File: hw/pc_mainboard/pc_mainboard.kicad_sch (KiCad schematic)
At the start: 0 parts

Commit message: Research for serial interface
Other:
- sheet ethernet renamed phy
- removed sheet program
- added sheet serial (serial.kicad_sch)
- sheet phy: file ethernet.kicad_sch -> phy.kicad_sch
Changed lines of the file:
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@@
 	(generator "eeschema")
 	(generator_version "8.0")
-	(paper "A4")
+	(paper "A2")
 	(title_block
 		(title "Mainboard")
 	)
 	(sheet
-		(at 53.34 81.28)
-		(size 36.83 29.21)
-		(fields_autoplaced yes)
-		(stroke
-			(width 0.1524)
-			(type solid)
-		)
-		(fill
-			(color 0 0 0 0.0000)
-		)
-		(property "Sheetname" "program"
-			(at 53.34 80.5684 0)
-			(effects
-				(font
-					(size 1.27 1.27)
-				)
-				(justify left bottom)
-			)
-		)
-		(property "Sheetfile" "program.kicad_sch"
-			(at 53.34 111.0746 0)
-			(effects
-				(font
-					(size 1.27 1.27)
-				)
-				(justify left top)
-			)
-		)
-		(instances
-			(project "pc_mainboard"
-				(path "/69a74940-cd00-4a75-bd5b-2bda9e86219a"
-					(page "8")
-				)
-			)
-		)
-	)
-	(sheet
-		(at 172.72 130.81)
+		(at 335.28 231.14)
 		(size 25.4 21.59)
 		(fields_autoplaced yes)
@@
 			(color 0 0 0 0.0000)
 		)
-		(property "Sheetname" "ethernet"
-			(at 172.72 130.0984 0)
-			(effects
-				(font
-					(size 1.27 1.27)
-				)
-				(justify left bottom)
-			)
-		)
-		(property "Sheetfile" "ethernet.kicad_sch"
-			(at 172.72 152.9846 0)
+		(property "Sheetname" "phy"
+			(at 335.28 230.4284 0)
+			(effects
+				(font
+					(size 1.27 1.27)
+				)
+				(justify left bottom)
+			)
+		)
+		(property "Sheetfile" "phy.kicad_sch"
+			(at 335.28 253.3146 0)
 			(effects
 				(font
@@
 	)
 	(sheet
-		(at 45.72 29.21)
+		(at 208.28 129.54)
 		(size 31.75 31.75)
 		(fields_autoplaced yes)
@@
 		)
 		(property "Sheetname" "power"
-			(at 45.72 28.4984 0)
+			(at 208.28 128.8284 0)
 			(effects
 				(font
@@
 		)
 		(property "Sheetfile" "power.kicad_sch"
-			(at 45.72 61.5446 0)
+			(at 208.28 161.8746 0)
 			(effects
 				(font
@@
 	)
 	(sheet
-		(at 134.62 29.21)
+		(at 297.18 129.54)
 		(size 36.83 31.75)
 		(fields_autoplaced yes)
@@
 		)
 		(property "Sheetname" "peripherals"
-			(at 134.62 28.4984 0)
+			(at 297.18 128.8284 0)
 			(effects
 				(font
@@
 		)
 		(property "Sheetfile" "peripherals.kicad_sch"
-			(at 134.62 61.5446 0)
+			(at 297.18 161.8746 0)
 			(effects
 				(font
@@
 	)
 	(sheet
-		(at 172.72 76.2)
+		(at 335.28 176.53)
 		(size 50.8 40.64)
 		(fields_autoplaced yes)
@@
 		)
 		(property "Sheetname" "flash"
-			(at 172.72 75.4884 0)
+			(at 335.28 175.8184 0)
 			(effects
 				(font
@@
 		)
 		(property "Sheetfile" "flash.kicad_sch"
-			(at 172.72 117.4246 0)
+			(at 335.28 217.7546 0)
 			(effects
 				(font
@@
 	)
 	(sheet
-		(at 111.76 76.2)
+		(at 274.32 176.53)
 		(size 45.72 40.64)
 		(fields_autoplaced yes)
@@
 		)
 		(property "Sheetname" "mpu"
-			(at 111.76 75.4884 0)
+			(at 274.32 175.8184 0)
 			(effects
 				(font
@@
 		)
 		(property "Sheetfile" "mpu.kicad_sch"
-			(at 111.76 117.4246 0)
+			(at 274.32 217.7546 0)
 			(effects
 				(font
@@
 	)
 	(sheet
-		(at 87.63 29.21)
+		(at 222.25 184.15)
+		(size 31.75 29.21)
+		(fields_autoplaced yes)
+		(stroke
+			(width 0.1524)
+			(type solid)
+		)
+		(fill
+			(color 0 0 0 0.0000)
+		)
+		(property "Sheetname" "serial"
+			(at 222.25 183.4384 0)
+			(effects
+				(font
+					(size 1.27 1.27)
+				)
+				(justify left bottom)
+			)
+		)
+		(property "Sheetfile" "serial.kicad_sch"
+			(at 222.25 213.9446 0)
+			(effects
+				(font
+					(size 1.27 1.27)
+				)
+				(justify left top)
+			)
+		)
+		(instances
+			(project "pc_mainboard"
+				(path "/69a74940-cd00-4a75-bd5b-2bda9e86219a"
+					(page "9")
+				)
+			)
+		)
+	)
+	(sheet
+		(at 250.19 129.54)
 		(size 38.1 31.75)
 		(fields_autoplaced yes)
@@
 		)
 		(property "Sheetname" "external"
-			(at 87.63 28.4984 0)
+			(at 250.19 128.8284 0)
 			(effects
 				(font
@@
 		)
 		(property "Sheetfile" "external.kicad_sch"
-			(at 87.63 61.5446 0)
+			(at 250.19 161.8746 0)
 			(effects
 				(font
@@
 	)
 	(sheet
-		(at 115.57 130.81)
+		(at 278.13 231.14)
 		(size 35.56 21.59)
 		(fields_autoplaced yes)
@@
 		)
 		(property "Sheetname" "ram"
-			(at 115.57 130.0984 0)
+			(at 278.13 230.4284 0)
 			(effects
 				(font
@@
 		)
 		(property "Sheetfile" "ram.kicad_sch"
-			(at 115.57 152.9846 0)
-			(effects
-				(font
+			(at 278.13 253.3146 0)
+			(effects
+				(font

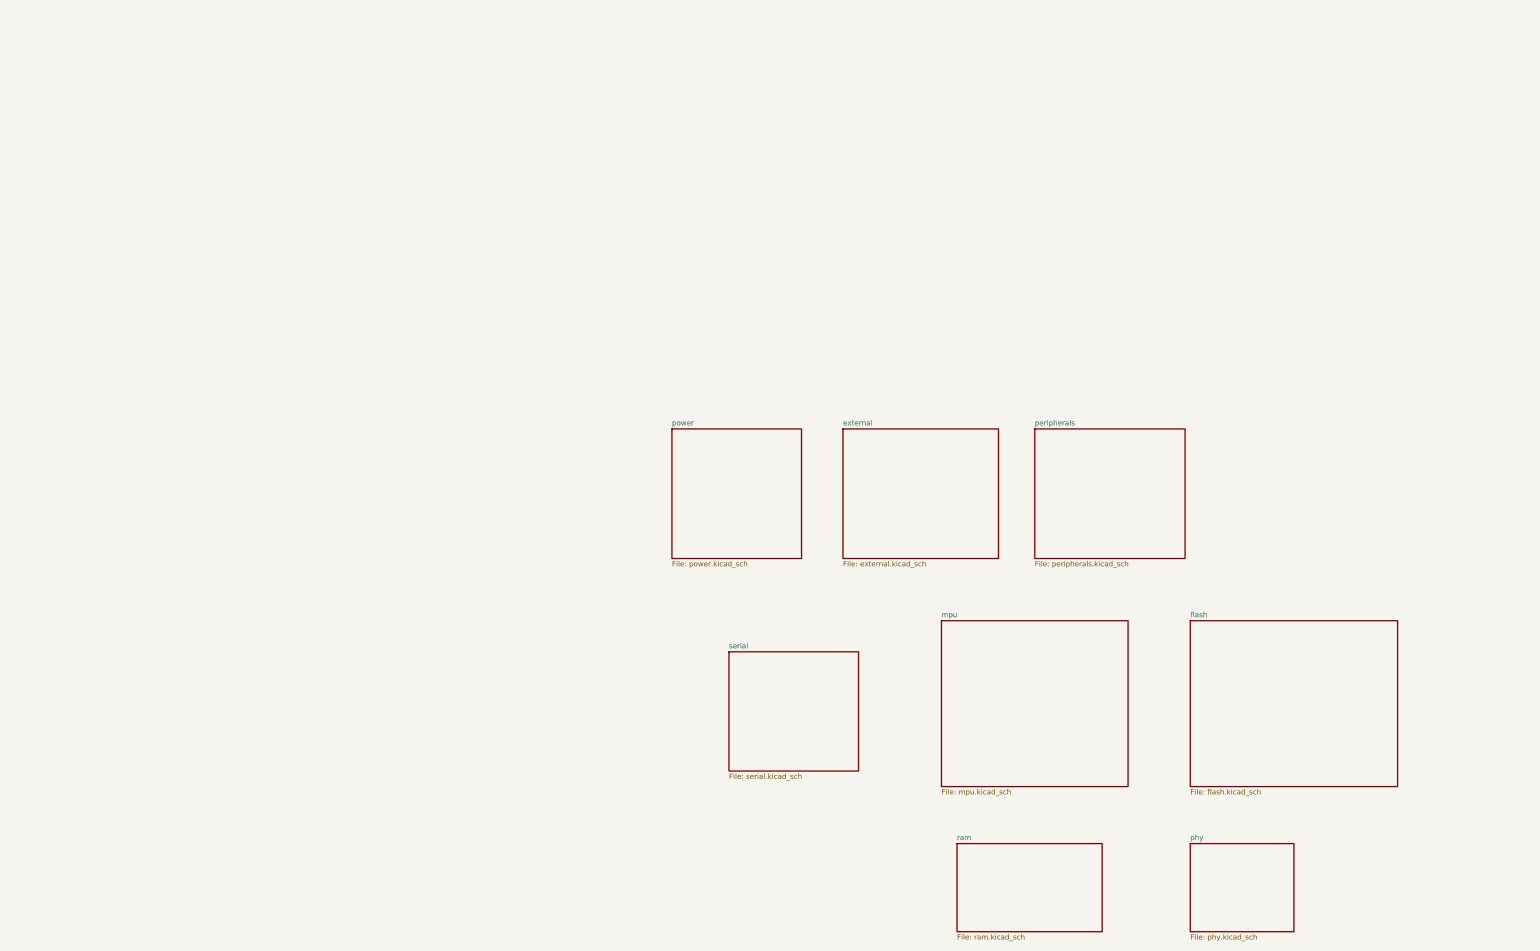
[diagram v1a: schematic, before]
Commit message: Added RTC (#22)
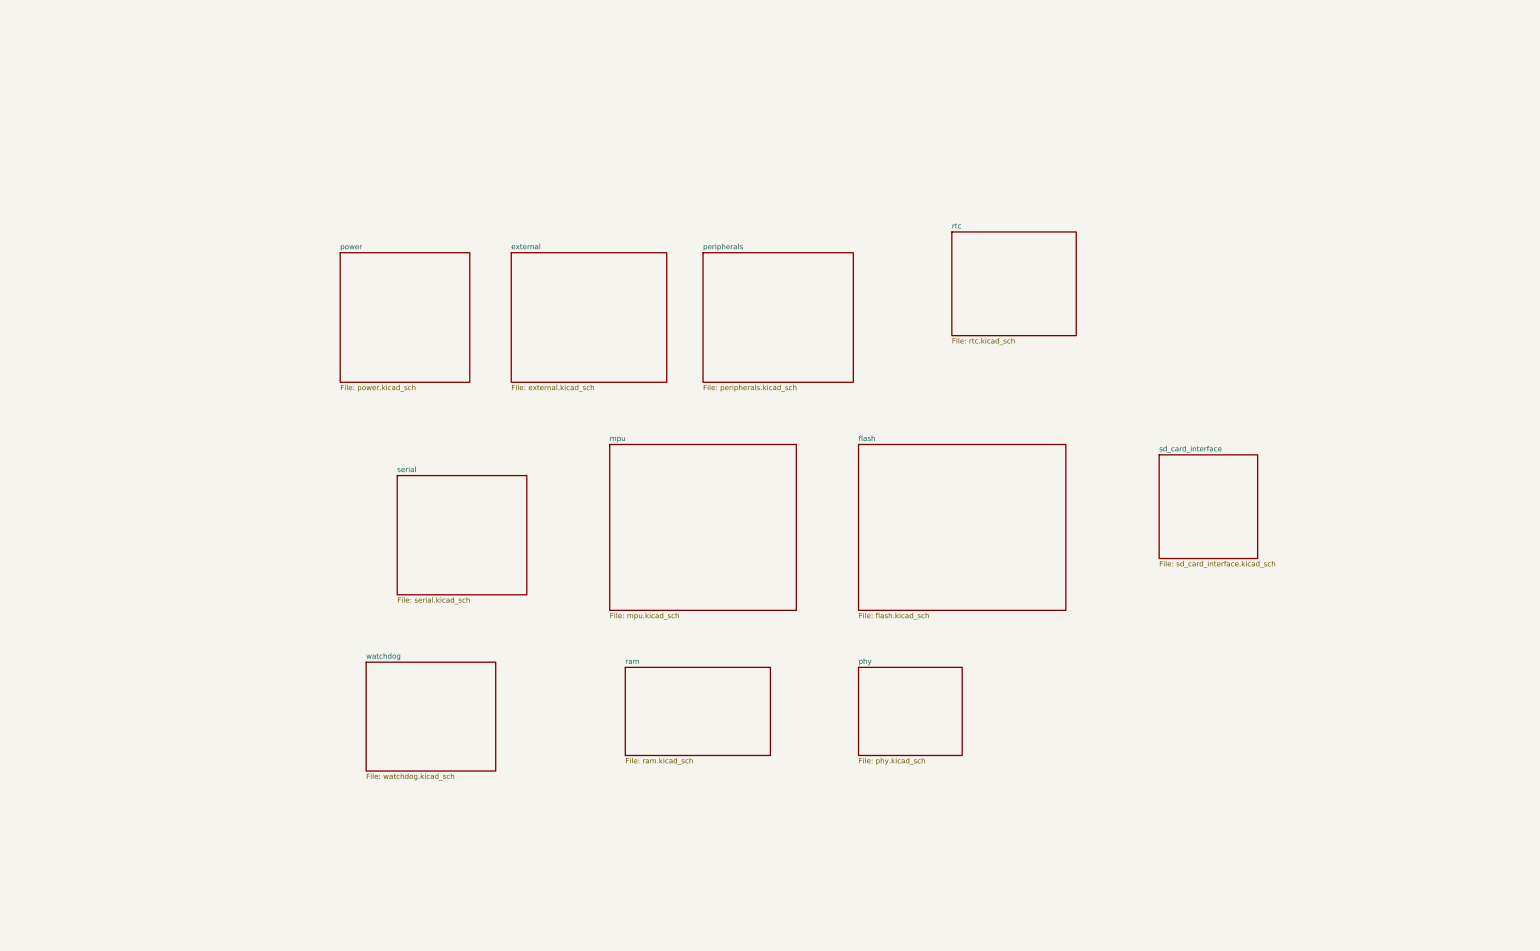
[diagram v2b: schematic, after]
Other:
- added sheet rtc (rtc.kicad_sch)
- added sheet sd_card_interface (sd_card_interface.kicad_sch)
- added sheet watchdog (watchdog.kicad_sch)
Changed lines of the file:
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@@
 	(generator "eeschema")
 	(generator_version "8.0")
-	(paper "A2")
+	(paper "B")
 	(title_block
 		(title "Mainboard")
 	)
 	(sheet
-		(at 335.28 231.14)
+		(at 276.86 81.28)
+		(size 30.48 25.4)
+		(fields_autoplaced yes)
+		(stroke
+			(width 0.1524)
+			(type solid)
+		)
+		(fill
+			(color 0 0 0 0.0000)
+		)
+		(property "Sheetname" "rtc"
+			(at 276.86 80.5684 0)
+			(effects
+				(font
+					(size 1.27 1.27)
+				)
+				(justify left bottom)
+			)
+		)
+		(property "Sheetfile" "rtc.kicad_sch"
+			(at 276.86 107.2646 0)
+			(effects
+				(font
+					(size 1.27 1.27)
+				)
+				(justify left top)
+			)
+		)
+		(instances
+			(project "pc_mainboard"
+				(path "/69a74940-cd00-4a75-bd5b-2bda9e86219a"
+					(page "10")
+				)
+			)
+		)
+	)
+	(sheet
+		(at 254 187.96)
 		(size 25.4 21.59)
 		(fields_autoplaced yes)
@@
 		)
 		(property "Sheetname" "phy"
-			(at 335.28 230.4284 0)
+			(at 254 187.2484 0)
 			(effects
 				(font
@@
 		)
 		(property "Sheetfile" "phy.kicad_sch"
-			(at 335.28 253.3146 0)
+			(at 254 210.1346 0)
 			(effects
 				(font
@@
 	)
 	(sheet
-		(at 208.28 129.54)
+		(at 327.66 135.89)
+		(size 24.13 25.4)
+		(fields_autoplaced yes)
+		(stroke
+			(width 0.1524)
+			(type solid)
+		)
+		(fill
+			(color 0 0 0 0.0000)
+		)
+		(property "Sheetname" "sd_card_interface"
+			(at 327.66 135.1784 0)
+			(effects
+				(font
+					(size 1.27 1.27)
+				)
+				(justify left bottom)
+			)
+		)
+		(property "Sheetfile" "sd_card_interface.kicad_sch"
+			(at 327.66 161.8746 0)
+			(effects
+				(font
+					(size 1.27 1.27)
+				)
+				(justify left top)
+			)
+		)
+		(instances
+			(project "pc_mainboard"
+				(path "/69a74940-cd00-4a75-bd5b-2bda9e86219a"
+					(page "12")
+				)
+			)
+		)
+	)
+	(sheet
+		(at 127 86.36)
 		(size 31.75 31.75)
 		(fields_autoplaced yes)
@@
 		)
 		(property "Sheetname" "power"
-			(at 208.28 128.8284 0)
+			(at 127 85.6484 0)
 			(effects
 				(font
@@
 		)
 		(property "Sheetfile" "power.kicad_sch"
-			(at 208.28 161.8746 0)
+			(at 127 118.6946 0)
 			(effects
 				(font
@@
 	)
 	(sheet
-		(at 297.18 129.54)
+		(at 215.9 86.36)
 		(size 36.83 31.75)
 		(fields_autoplaced yes)
@@
 		)
 		(property "Sheetname" "peripherals"
-			(at 297.18 128.8284 0)
+			(at 215.9 85.6484 0)
 			(effects
 				(font
@@
 		)
 		(property "Sheetfile" "peripherals.kicad_sch"
-			(at 297.18 161.8746 0)
+			(at 215.9 118.6946 0)
 			(effects
 				(font
@@
 	)
 	(sheet
-		(at 335.28 176.53)
+		(at 254 133.35)
 		(size 50.8 40.64)
 		(fields_autoplaced yes)
@@
 		)
 		(property "Sheetname" "flash"
-			(at 335.28 175.8184 0)
+			(at 254 132.6384 0)
 			(effects
 				(font
@@
 		)
 		(property "Sheetfile" "flash.kicad_sch"
-			(at 335.28 217.7546 0)
+			(at 254 174.5746 0)
 			(effects
 				(font
@@
 	)
 	(sheet
-		(at 274.32 176.53)
+		(at 133.35 186.69)
+		(size 31.75 26.67)
+		(fields_autoplaced yes)
+		(stroke
+			(width 0.1524)
+			(type solid)
+		)
+		(fill
+			(color 0 0 0 0.0000)
+		)
+		(property "Sheetname" "watchdog"
+			(at 133.35 185.9784 0)
+			(effects
+				(font
+					(size 1.27 1.27)
+				)
+				(justify left bottom)
+			)
+		)
+		(property "Sheetfile" "watchdog.kicad_sch"
+			(at 133.35 213.9446 0)
+			(effects
+				(font
+					(size 1.27 1.27)
+				)
+				(justify left top)
+			)
+		)
+		(instances
+			(project "pc_mainboard"
+				(path "/69a74940-cd00-4a75-bd5b-2bda9e86219a"
+					(page "11")
+				)
+			)
+		)
+	)
+	(sheet
+		(at 193.04 133.35)
 		(size 45.72 40.64)
 		(fields_autoplaced yes)
@@
 		)
 		(property "Sheetname" "mpu"
-			(at 274.32 175.8184 0)
+			(at 193.04 132.6384 0)
 			(effects
 				(font
@@
 		)
 		(property "Sheetfile" "mpu.kicad_sch"
-			(at 274.32 217.7546 0)
+			(at 193.04 174.5746 0)
 			(effects
 				(font
@@
 	)
 	(sheet
-		(at 222.25 184.15)
+		(at 140.97 140.97)
 		(size 31.75 29.21)
 		(fields_autoplaced yes)
@@
 		)
 		(property "Sheetname" "serial"
-			(at 222.25 183.4384 0)
+			(at 140.97 140.2584 0)
 			(effects
 				(font
@@
 		)
 		(property "Sheetfile" "serial.kicad_sch"
-			(at 222.25 213.9446 0)
+			(at 140.97 170.7646 0)
 			(effects
 				(font
@@
 	)
 	(sheet
-		(at 250.19 129.54)
+		(at 168.91 86.36)
 		(size 38.1 31.75)
 		(fields_autoplaced yes)
@@
 		)
 		(property "Sheetname" "external"
-			(at 250.19 128.8284 0)
+			(at 168.91 85.6484 0)
 			(effects
 				(font
@@
 		)
 		(property "Sheetfile" "external.kicad_sch"
-			(at 250.19 161.8746 0)
+			(at 168.91 118.6946 0)
 			(effects
 				(font
@@
 	)
 	(sheet
-		(at 278.13 231.14)
+		(at 196.85 187.96)
 		(size 35.56 21.59)
 		(fields_autoplaced yes)
@@
 		)
 		(property "Sheetname" "ram"
-			(at 278.13 230.4284 0)
+			(at 196.85 187.2484 0)
 			(effects
 				(font
@@
 		)
 		(property "Sheetfile" "ram.kicad_sch"
-			(at 278.13 253.3146 0)
-			(effects
-				(font
+			(at 196.85 210.1346 0)
+			(effects
+				(font

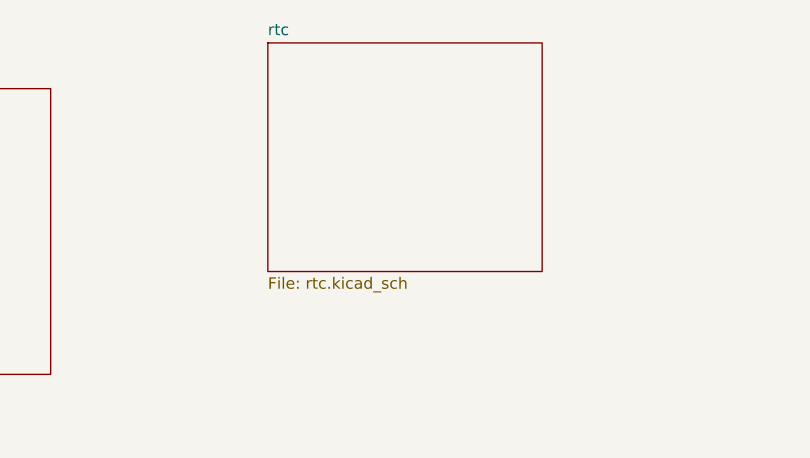
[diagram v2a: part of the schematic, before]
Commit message: RTC Schematic Capture (#35)
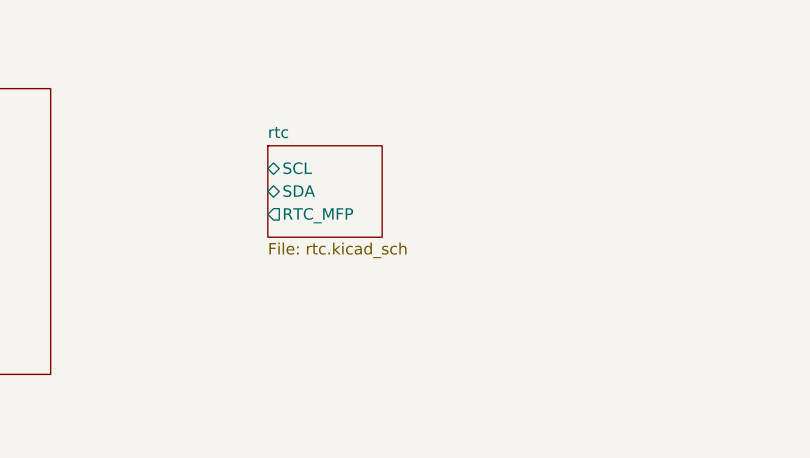
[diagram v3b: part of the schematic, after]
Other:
- sheet rtc ports: added RTC_MFP, SCL, SDA; removed none
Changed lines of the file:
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@@
 	)
 	(sheet
-		(at 276.86 81.28)
-		(size 30.48 25.4)
+		(at 276.86 92.71)
+		(size 12.7 10.16)
 		(fields_autoplaced yes)
 		(stroke
@@
 		)
 		(property "Sheetname" "rtc"
-			(at 276.86 80.5684 0)
+			(at 276.86 91.9984 0)
 			(effects
 				(font
@@
 		)
 		(property "Sheetfile" "rtc.kicad_sch"
-			(at 276.86 107.2646 0)
+			(at 276.86 103.4546 0)
 			(effects
 				(font
@@
 			)
 		)
+		(pin "RTC_MFP" output
+			(at 276.86 100.33 180)
+			(effects
+				(font
+					(size 1.27 1.27)
+				)
+				(justify left)
+			)
+		)
+		(pin "SDA" bidirectional
+			(at 276.86 97.79 180)
+			(effects
+				(font
+					(size 1.27 1.27)
+				)
+				(justify left)
+			)
+		)
+		(pin "SCL" bidirectional
+			(at 276.86 95.25 180)
+			(effects
+				(font
+					(size 1.27 1.27)
+				)
+				(justify left)
+			)
+		)

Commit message: EEPROM Research (#36)
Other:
- added sheet eeprom (eeprom.kicad_sch)
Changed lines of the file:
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@@
+	)
+	(sheet
+		(at 321.31 92.71)
+		(size 22.86 24.13)
+		(fields_autoplaced yes)
+		(stroke
+			(width 0.1524)
+			(type solid)
+		)
+		(fill
+			(color 0 0 0 0.0000)
+		)
+		(property "Sheetname" "eeprom"
+			(at 321.31 91.9984 0)
+			(effects
+				(font
+					(size 1.27 1.27)
+				)
+				(justify left bottom)
+			)
+		)
+		(property "Sheetfile" "eeprom.kicad_sch"
+			(at 321.31 117.4246 0)
+			(effects
+				(font
+					(size 1.27 1.27)
+				)
+				(justify left top)
+			)
+		)
+		(instances
+			(project "pc_mainboard"
+				(path "/69a74940-cd00-4a75-bd5b-2bda9e86219a"
+					(page "13")
+				)
+			)
+		)
 	)
 	(sheet
